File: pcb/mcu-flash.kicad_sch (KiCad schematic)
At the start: 30 parts, among them J1 0015910100, SW1 EVQ-P7J01P, SW2 TS04-66-50-BK-160-SMT, U1 W25Q128JVS, U2 RP2040, Y1 ABM8AIG-12.000MHZ-12-2Z-T3

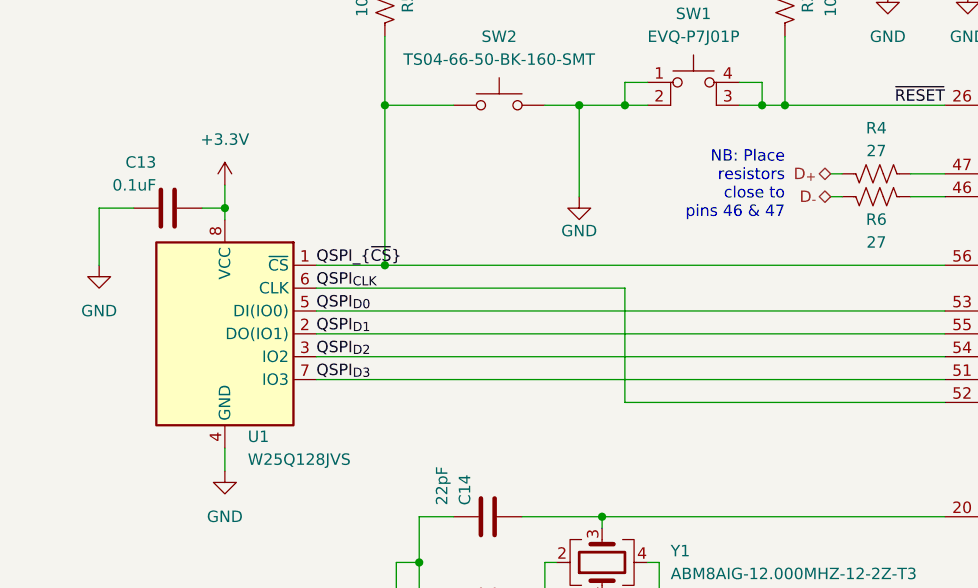
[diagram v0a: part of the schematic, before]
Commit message: Add USB diode protection
- Change revision g -> h
  - schematic
  - pcb
  - silk screen
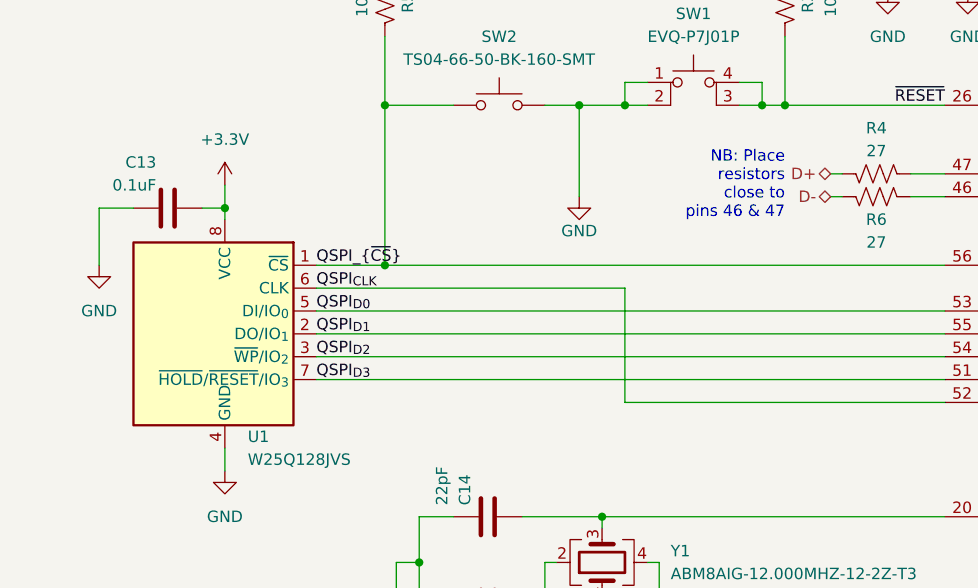
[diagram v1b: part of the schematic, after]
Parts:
- U1: footprint Package_SO:SOIC-8_5.23x5.23mm_P1.27mm -> Package_SO:SOIC-8_5.3x5.3mm_P1.27mm
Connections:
- net D_{+} renamed D+
- net D_{-} renamed D-
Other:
- moved on the sheet: U1
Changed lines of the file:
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@@
 (kicad_sch
-	(version 20241209)
+	(version 20250114)
 	(generator "eeschema")
 	(generator_version "9.0")
@@
 	(title_block
 		(title "Open Ephys Commutator Controller")
-		(rev "G")
+		(rev "H")
 		(company "Open Ephys, Inc.")
 		(comment 1 "Cris Sharp")
@@
 			"tkw1D4fDwcyZM9G1a1c2RTHNCsApiqIoiqIoimoeeg84RVEURVEURbUiGoBTFEVRFEVRVCuiAThF"
 			"URRFURRFtSIagFMURVEURVFUK6IBOEVRFEVRFEW1IhqAUxRFURRFUVQrogE4RVEURVEURbUa4P8B"
-			"65C3O7MQdOoAAAAASUVORK5CYII="
+			"65C3O7MQdOoAAAAASUVORK5CYIIAAAAAAAAAAAAAAAAAAAAAAAAAAAAAAAAAAAAAAAAAAAAAAAAA"
+			"AAAAAAAAAAAAAAAAAAAAAAAAAAAAAAAAAAAAAAAAAAAAAAAAAAAAAAAAAAAAAAAAAAAAAAAAAAAA"
+			"AAAAAAAAAAAAAAAAAAAAAAAAAAAAAAAAAAAAAAAAAAAAAAAAAAAAAAAAAAAAAAAAAAAAAAAAAAAA"
+			"AAAAAAAAAAAAAAAAAAAAAAAAAAAAAAAAAAAAAAAAAAAAAAAAAAAAAAAAAAAAAAAAAAAAAAAAAAAA"
+			"AAAAAAAAAAAAAAAAAAAAAAAAAAAAAAAAAAAAAAAAAAAAAAAAAAAAAAAAAAAAAAAAAAAAAAAAAAAA"
+			"AAAAAAAAAAAAAAAAAAAAAAAAAAAAAAAAAAAAAAAAAAAAAAAAAAAAAAAAAAAAAAAAAAAAAAAAAAAA"
+			"AAAAAAAAAAAAAAAAAAAAAAAAAAAAAAAAAAAAAAAAAAAAAAAAAAAAAAAAAAAAAAAAAAAAAAAAAAAA"
+			"AAAAAAAAAAAAAAAAAAAAAAAAAAAAAAAAAAAAAAAAAAAAAAAAAAAAAAAAAAAAAAAAAAAAAAAAAAAA"
+			"AAAAAAAAAAAAAAAAAAAAAAAAAAAAAAAAAAAAAAAAAAAAAAAAAAAAAAAAAAAAAAAAAAAAAAAAAAAA"
+			"AAAAAAAAAAAAAAAAAAAAAAAAAAAAAAAAAAAAAAAAAAAAAAAAAAAAAAAAAAAAAAAAAAAAAAAAAAAA"
+			"AAAAAAAAAAAAAAAAAAAAAAAAAAAAAAAAAAAAAAAAAAAAAAAAAAAAAAAAAAAAAAAAAAAAAAAAAAAA"
+			"AAAAAAAAAAAAAAAAAAAAAAAAAAAAAAAAAAAAAAAAAAAAAAAAAAAAAAAAAAAAAAAAAAAAAAAAAAAA"
+			"AAAAAAAAAAAAAAAAAAAAAAAAAAAAAAAAAAAAAAAAAAAAAAAAAAAAAAAAAAAAAAAAAAAAAAAAAAAA"
+			"AAAAAAAAAAAAAAAAAAAAAAAAAAAAAAAAAAAAAAAAAAAAAAAAAAAAAAAAAAAAAAAAAAAAAAAAAAAA"
+			"AAAAAAAAAAAAAAAAAAAAAAAAAAAAAAAAAAAAAAAAAAAAAAAAAAAAAAAAAAAAAAAAAAAAAAAAAAAA"
+			"AAAAAAAAAAAAAAAAAAAAAAAAAAAAAAAAAAAAAAAAAAAAAAAAAAAAAAAAAAAAAAAAAAAAAAAAAAAA"
+			"AAAAAAAAAAAAAAAAAAAAAAAAAAAAAAAAAAAAAAAAAAAAAAAAAAAAAAAAAAAAAAAAAAAAAAAAAAAA"
+			"AAAAAAAAAAAAAAAAAAAAAAAAAAAAAAAAAAAAAAAAAAAAAAAAAAAAAAAAAAAAAAAAAAAAAAAAAAAA"
+			"AAAAAAAAAAAAAAAAAAAAAAAAAAAAAAAAAAAAAAAAAAAAAAAAAAAAAAAAAAAAAAAAAAAAAAAAAAAA"
+			"AAAAAAAAAAAAAAAAAAAAAAAAAAAAAAAAAAAAAAAAAAAAAAAAAAAAAAAAAAAAAAAAAAAAAAAAAAAA"
+			"AAAAAAAAAAAAAAAAAAAAAAAAAAAAAAAAAAAAAAAAAAAAAAAAAAAAAAAAAAAAAAAAAAAAAAAAAAAA"
+			"AAAAAAAAAAAAAAAAAAAAAAAAAAAAAAAAAAAAAAAAAAAAAAAAAAAAAAAAAAAAAAAAAAAAAAAAAAAA"
+			"AAAAAAAAAAAAAAAAAAAAAAAAAAAAAAAAAAAAAAAAAAAAAAAAAAAAAAAAAAAAAAAAAAAAAAAAAAAA"
+			"AAAAAAAAAAAAAAAAAAAAAAAAAAAAAAAAAAAAAAAAAAAAAAAAAAAAAAAAAAAAAAAAAAAAAAAAAAAA"
+			"AAAAAAAAAAAAAAAAAAAAAAAAAAAAAAAAAAAAAAAAAAAAAAAAAAAAAAAAAAAAAAAAAAAAAAAAAAAA"
+			"AAAAAAAAAAAAAAAAAAAAAAAAAAAAAAAAAAAAAAAAAAAAAAAAAAAAAAAAAAAAAAAAAAAAAAAAAAAA"
+			"AAAAAAAAAAAAAAAAAAAAAAAAAAAAAAAAAAAAAAAAAAAAAAAAAAAAAAAAAAAAAAAAAAAAAAAAAAAA"
+			"AAAAAAAAAAAAAAAAAAAAAAAAAAAAAAAAAAAAAAAAAAAAAAAAAAAAAAAAAAAAAAAAAAAAAAAAAAAA"
+			"AAAAAAAAAAAAAAAAAAAAAAAAAAAAAAAAAAAAAAAAAAAAAAAAAAAAAAAAAAAAAAAAAAAAAAAAAAAA"
+			"AAAAAAAAAAAAAAAAAAAAAAAAAAAAAAAAAAAAAAAAAAAAAAAAAAAAAAAAAAAAAAAAAAAAAAAAAAAA"
+			"AAAAAAAAAAAAAAAAAAAAAAAAAAAAAAAAAAAAAAAAAAAAAAAAAAAAAAAAAAAAAAAAAAAAAAAAAAAA"
+			"AAAAAAAAAAAAAAAAAAAAAAAAAAAAAAAAAAAAAAAAAAAAAAAAAAAAAAAAAAAAAAAAAAAAAAAAAAAA"
+			"AAAAAAAAAAAAAAAAAAAAAAAAAAAAAAAAAAAAAAAAAAAAAAAAAAAAAAAAAAAAAAAAAAAAAAAAAAAA"
+			"AAAAAAAAAAAAAAAAAAAAAAAAAAAAAAAAAAAAAAAAAAAAAAAAAAAAAAAAAAAAAAAAAAAAAAAAAAAA"
+			"AAAAAAAAAAAAAAAAAAAAAAAAAAAAAAAAAAAAAAAAAAAAAAAAAAAAAAAAAAAAAAAAAAAAAAAAAAAA"
+			"AAAAAAAAAAAAAAAAAAAAAAAAAAAAAAAAAAAAAAAAAAAAAAAAAAAAAAAAAAAAAAAAAAAAAAAAAAAA"
+			"AAAAAAAAAAAAAAAAAAAAAAAAAA=="
 		)
 	)
@@
 			"nn16oXsDE20RirS9sXGrXrG8QahA26gnrKx6yKyjqfMThfpcLvLjw/96ztAkpkKhUCgUCoVCoVDe"
 			"hSbbFAqFQqFQKBRKM0GTbQqFQqFQKBQKpZmgyTaFQqFQKBQKhdIsAP8fPZc3Zc/CT3kAAAAASUVO"
-			"RK5CYII="
+			"RK5CYIJsADYAQQBpAGUANABwAC8ARAAvAHIAagBMAFoAWQByAEUAQgBNAGkANgBmAEEATABIAHIA"
+			"eABhAGcAcQB3ADYANwAyAGYAZQBUAFIAWgAyAGwAMQBjAHEAdgB4AFAAdAA3AHkAVQBPADMAdQAr"
+			"AGkAawByAG0AUgBzACsAaAAvAGIAaABwAC8AKwBwAHUAZAB2AHkAWgAvAFEAaABIAGcAZABkAHgA"
+			"awBYAHIAcQBXAEEASwAxADIATgBqAGsAaAAwAEIAOABuAFcAMgByAFYAcgBGADUAVwBYAGwAOABj"
+			"ADgAcQA4AEsAbgBuAGgAMgBkAFQAZABsAC8ATQBJAEoAYQBkAFkAbgBMAGwASABWAE0ATwAzAGIA"
+			"cwBvAEEASQBEAEEANQBsAG4AVgBmAGgAVQAyAHAARwBaAGwATQBPAG4ATwA2AGoAWQA2AHUAcgB6"
+			"AHEAYwB4AFQAOAA2AG4AaABMAGgAdQBvAHEAeABVAFUAOQBlAGIANgBSAHMAcgBGAFkAVABGADEA"
+			"dgBwAFIAWgBMAEYASgAyAGwALwByAHAAMAA2AEgAVQB0AEUAUABKAEYATQBWAEwAcABQAFoAUABj"
+			"AGEAQgBtAEgAawBtAGoALwA1AEsAaQBDAGcATgA4AHEASgBIAGoATgBsAEUAMwB5AGkAVQB2ADUA"
+			"VAAvAC8AZwA1AG8ANwB6AEkAdgBhAG4AOABpAFQARgBGAFQAagBVADgAOQBQAEwAYQBCAEcAdQBL"
+			"ADYAawBRAGwANABKAG0ARABMADYAcgBXAE8AMgBVADUANABPADAANgBqADkAUwBUAHkASwBuADMA"
+			"YQBFAG0AdQBuAHcASwBiAFcAagBwAG4ASQBVAFAALwBNAFUATgBYACsANABDADcAVgBCAFYARABs"
+			"ACsATwBWAFcAWQBWADAAUgBWAGkAUAA2AGMAVgAwAFkAVgBsAFgAQwBwAG0AbgBkAHEAdgBYAFgA"
+			"cgAxAGwARQBaAEcAUgBuAE0ATQB3AGIALwBPAFgAWABzAEMAMABkAHEANgB2ADQAawBTAG4AbwBM"
+			"AGUAQQBuADcAcQBNAGsATwBzADYAZwBqAHoAMABSAGIAegBjAGcAUABvAHAAWQA3AGYAVQBZAHQA"
+			"WAB6AEcARgBHAHIAMwBrAEgAeQBwAFgAcQBqAEkATgB0AFcATgBGAHoARQAvAFUAcAAwAE8AbgBV"
+			"AGIAOABsAFMANwA5AHoAQgBYAFgAeABtAHgASABVADYATABYAGgAVgBLADIASQA0AGkAVgBRAGYA"
+			"LwArADgAaAAvAEsATABTAHEAUgBpADkAawArAGoASABPAGYAOABRAFcAVgBLAHIAVgBwAGEAOAAr"
+			"AHMAUwBVAEkAVgBSAEcAeQBoADMAQgAwADkAcQBSADMAUQBaAFIAWABIAGoAcQBGACsAbgBPAGwA"
+			"SQB1AHEAeQAvAFYAcQByAE0AcwBaAEcAVgBsAFUAZAA5AC8ALwB6ADMAegBUAEIAcQBQAFMAdAB3"
+			"AC8AaABYAEsAWQBlAFkAUgBLAG8ANwBlAGoASQB2AEoANwB5AG4AbgAwAEMAaQBvADQAbgA2AGsA"
+			"QQBQADQAMAA2ADcATwAxAEEAZQBlADYATwBvAHkAcABiAEUAQwB0ADAANABGAEUAKwBJADgAZABS"
+			"AG0AMgBvAEMAagAvAHAAagA3AGoARABLAGEAMwA5AGkAcgBYADYAagBGAHoAUQBiADgALwB6AG4A"
+			"cAA2AGcARgBJADEAeQBwAGwAUwBHAHYAYQB1AEsAcABMAEkAYgBhADcAdQBsAEEAVABhAFAAagBn"
+			"AEcANQBoADYAdgBwAEcARgA4AHIAaABQACsAZQBvAEkAcwBuAFMAdAA1AEsAZgBuADkAOQBJAEcA"
+			"egBIAHIAVwBYAHkAZQBxAGoAMwA4AEoASAAxADUASwBKAGwATABwAFIAMgBlAFMAVABsADYAKwAx"
+			"AEsAcAA0AGwAagBnAFUANgBtACsATQA2AGsAUgBZADgAZABTAG8ANwA2AHMAaQBvADkASwA2AHYA"
+			"NwBQAEUANgBsAGgALwArADkAUABLAGsAYwBnAGUAagA5AFgAYQBzAFEAWQBKADIAcQA0AHgAMAA5"
+			"AFUAZABLADAAQQBLADYATwB1AGIAdgBpAEUARwB1AGsAOABsAGwANgAyAG4AYgBwAFgAMgBWAHkA"
+			"ZgAxAFAASABtAE8AcgBYAFIAeABZAEYAYQBMAEIAVgAwAGcAdAB3AHoAMQBGAGUATwByAHQAUQBQ"
+			"AE4AOQA0AHcASgBTADEAMwA2AE4AQQBoADYAdABpAHgAWQA4AHkAegBLAHMAMwAzAEgAUwA5AHgA"
+			"UAB6AFgARgBZAFMAWgAxAFIAQgBSAFUAZABPADkAbAAvAGYAMQBmAGEAdQBUAFkAcABkAFMANQA1"
+			"AHoAVgBSAFUAQgBLADcAbQAvAEkAYQA5AGkAbQAxAFAAYQBaAFcAQQA3AFIASQBlAEgAZwA0AHQA"
+			"VwAzAGIATgB1AGEAWgBsAEEAYQAyAFgAOQBTAG0AZAAzAC8ANgBsAEIAbwA2ADcAUgBDAFYAegBL"
+			"AHMAZAA3ADUAUQBnAGkALwByADcAdgB5AE8AcABzAFUAdgBQAFUAVABWAFYASwA2AEYAaQBkADMA"
+			"dABSAHcAegA3AGQAVABrAG0AcQBWAGsAZwBGACsASQB5AGsAeABtADIANgBRAFUAbQBpAG0AaAA0"
+			"AEgAZg=="
 		)
 	)
@@
 		)
 	)
-	(hierarchical_label "D_{+}"
+	(hierarchical_label "D+"
 		(shape bidirectional)
 		(at 104.14 71.12 180)
@@
 		)
 	)
-	(hierarchical_label "D_{-}"
+	(hierarchical_label "D-"
 		(shape bidirectional)
 		(at 104.14 73.66 180)
@@
 			)
 		)
-		(property "Footprint" "Package_SO:SOIC-8_5.23x5.23mm_P1.27mm"
-			(at 36.83 88.9 0)
+		(property "Footprint" "Package_SO:SOIC-8_5.3x5.3mm_P1.27mm"
+			(at 36.83 66.04 0)
 			(effects
 				(font
@@
 		)
 		(property "Datasheet" "https://www.winbond.com/resource-files/w25q128jv_dtr%20revc%2003272018%20plus.pdf"
-			(at 36.83 88.9 0)
+			(at 36.83 63.5 0)
 			(effects
 				(font
@@
 			)
 		)
-		(property "Description" "128Mb Serial Flash Memory, Standard/Dual/Quad SPI, SOIC-8"
-			(at 36.83 88.9 0)
+		(property "Description" "128Mbit / 16MiB Serial Flash Memory, Standard/Dual/Quad SPI, 2.7-3.6V, SOIC-8"
+			(at 36.83 60.96 0)
 			(effects
 				(font

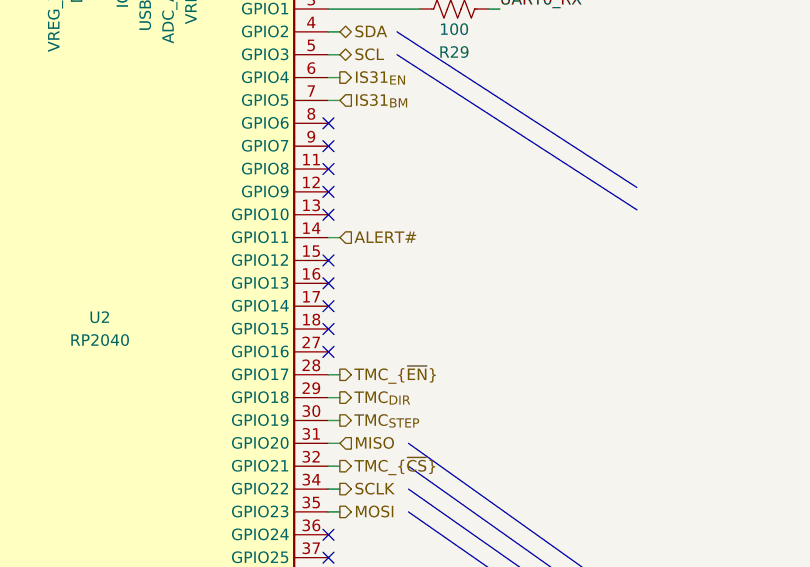
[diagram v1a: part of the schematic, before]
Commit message: Lower sense resistance (0.5 -> 0.43 Ohms)
Also:
- Route TMC2130 diagnostic pins to RP2040
- Instead of manually excluding violations:
  - Changed spoke minimum: 2 -> 1
  - Changed copper-to-hole clearance: 0.25mm -> 0.19mm
- Update revision labels on sch, pcb, and silkscreen
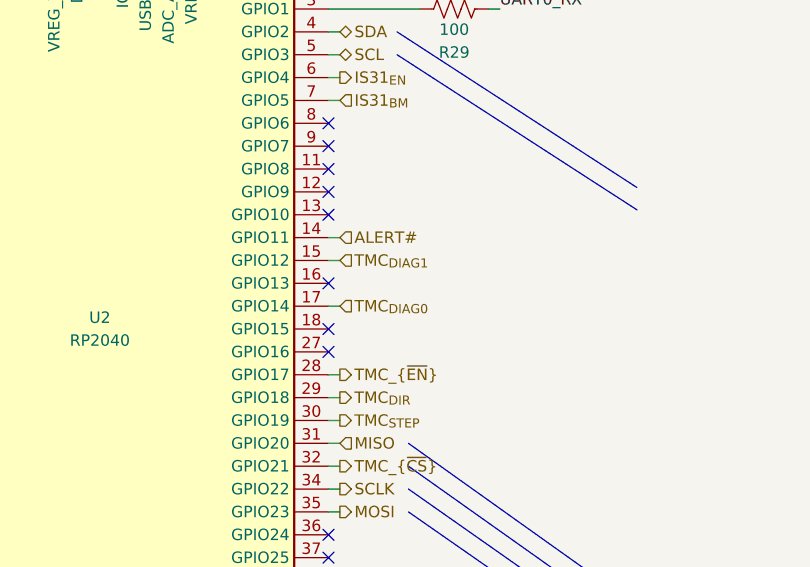
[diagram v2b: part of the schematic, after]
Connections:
- net TMC_{DIAG1}: now reaches U2.15 (GPIO12)
- net TMC_{DIAG0}: now reaches U2.17 (GPIO14)
- no-connect marks 12 -> 10
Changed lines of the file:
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@@
 	)
 	(no_connect
-		(at 167.64 93.98)
-	)
-	(no_connect
 		(at 167.64 78.74)
 	)
@@
 	)
 	(no_connect
-		(at 167.64 99.06)
-	)
-	(no_connect
 		(at 167.64 96.52)
 	)
@@
 	(wire
 		(pts
+			(xy 168.91 99.06) (xy 167.64 99.06)
+		)
+		(stroke
+			(width 0)
+			(type default)
+		)
+	)
+	(wire
+		(pts
 			(xy 96.52 60.96) (xy 96.52 63.5)
 		)
@@
 	(wire
 		(pts
+			(xy 167.64 93.98) (xy 168.91 93.98)
+		)
+		(stroke
+			(width 0)
+			(type default)
+		)
+	)
+	(wire
+		(pts
 			(xy 156.21 41.91) (xy 156.21 40.64)
 		)
@@
 		)
 	)
+	(hierarchical_label "TMC_{DIAG1}"
+		(shape input)
+		(at 168.91 93.98 0)
+		(effects
+			(font
+				(size 1.27 1.27)
+			)
+			(justify left)
+		)
+	)
 	(hierarchical_label "LTC44_{~{PFO}}"
 		(shape input)
@@
 		(effects
 			(font
+				(size 1.27 1.27)
+			)
+			(justify left)
+		)
+	)
+	(hierarchical_label "TMC_{DIAG0}"
+		(shape input)
+		(at 168.91 99.06 0)
+		(effects
+			(font

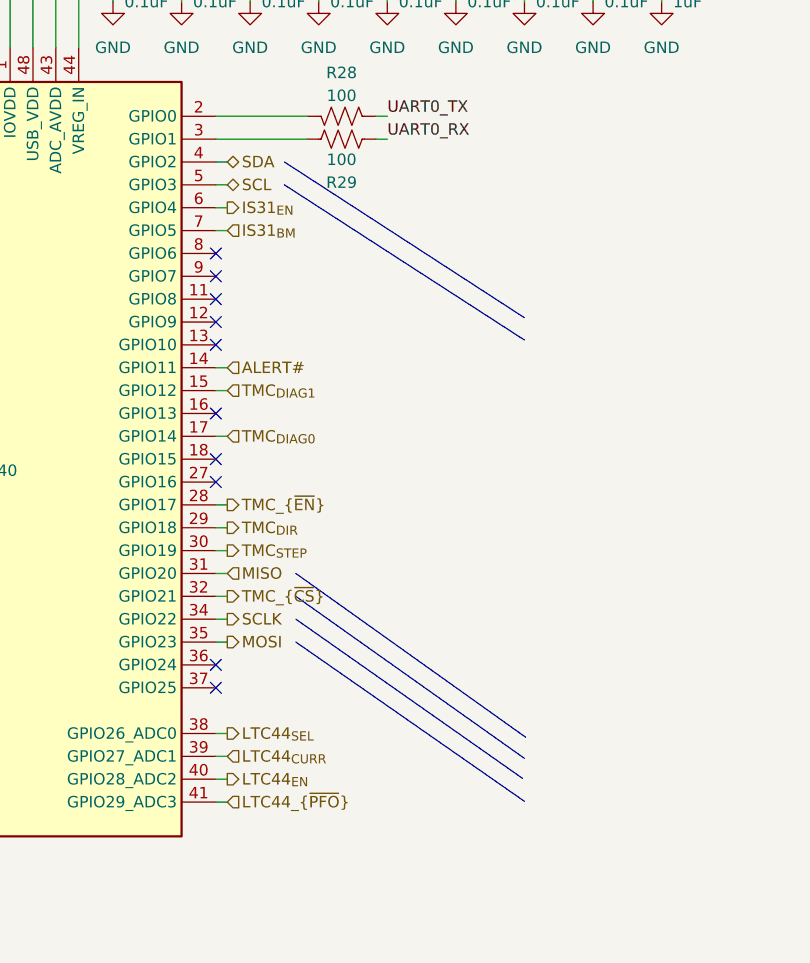
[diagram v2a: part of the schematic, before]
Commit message: Small updates during review
- Schematic clarifications
- Update footprints to match library latest
- Small silkscreen and via positioning changes to support clean
  silkscreen
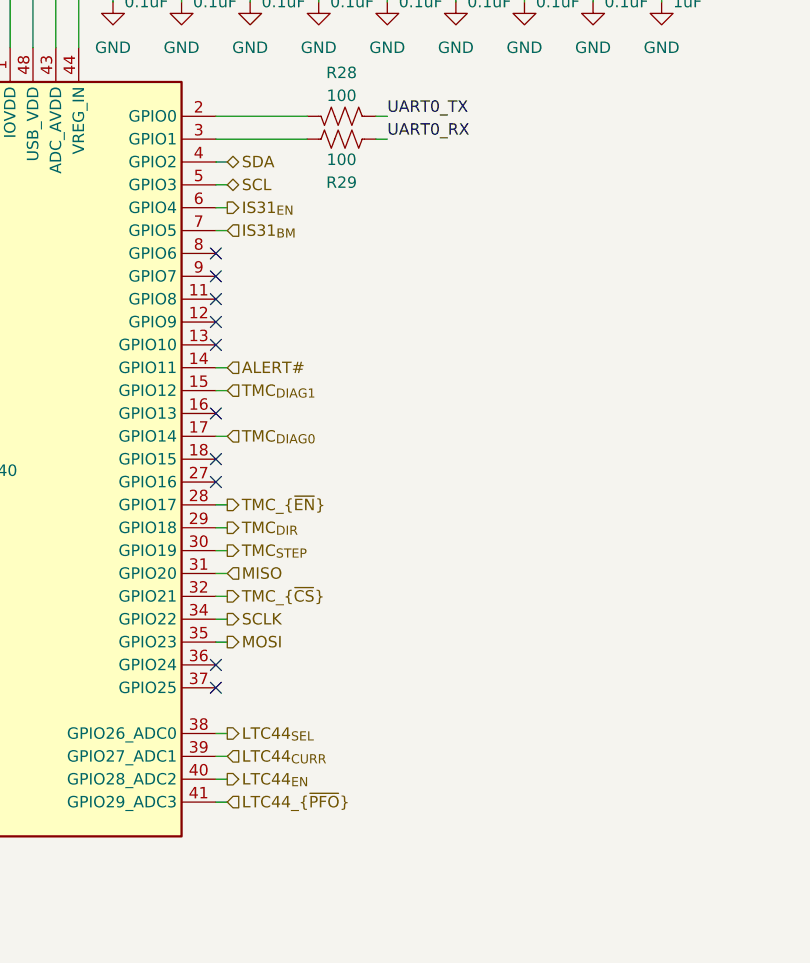
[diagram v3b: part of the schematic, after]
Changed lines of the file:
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@@
 	(title_block
 		(title "Open Ephys Commutator Controller")
-		(rev "H")
+		(rev "J")
 		(company "Open Ephys, Inc.")
 		(comment 1 "Cris Sharp")
@@
 		)
 	)
-	(polyline
-		(pts
-			(xy 201.9122 139.6053) (xy 176.53 121.92)
-		)
-		(stroke
-			(width 0)
-			(type default)
-		)
-	)
 	(wire
 		(pts
@@
 		)
 	)
-	(polyline
-		(pts
-			(xy 176.53 114.3) (xy 202.0507 132.4883)
-		)
-		(stroke
-			(width 0)
-			(type default)
-		)
-	)
 	(wire
 		(pts
@@
 		)
 	)
-	(polyline
-		(pts
-			(xy 175.26 68.58) (xy 201.9004 85.8664)
-		)
-		(stroke
-			(width 0)
-			(type default)
-		)
-	)
 	(wire
 		(pts
@@
 		)
 	)
-	(polyline
-		(pts
-			(xy 201.9122 134.833) (xy 176.53 116.84)
-		)
-		(stroke
-			(width 0)
-			(type default)
-		)
-	)
 	(wire
 		(pts
@@
 		)
 	)
-	(polyline
-		(pts
-			(xy 176.53 119.38) (xy 201.7205 137.07)
-		)
-		(stroke
-			(width 0)
-			(type default)
-		)
-	)
 	(wire
 		(pts
@@
 		)
 		(stroke
-			(width 0)
-			(type default)
-		)
-	)
-	(polyline
-		(pts
-			(xy 175.26 71.12) (xy 201.9217 88.359)
-		)
-		(stroke
